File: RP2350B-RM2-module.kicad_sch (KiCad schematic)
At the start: 58 parts, among them J1 SM03B-SRSS-TB, J2 Conn_01x26_Socket, J3 Conn_01x26_Socket, J5 USB_C_Receptacle_USB2.0_16P, SW1 SW_Push, SW2 SW_Push, U1 W25Q128JVSIQ, U2 APS6404L-3SQR-SN, U3 RP2350_80QFN, U4 RM2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

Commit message: clean ERC and DRC
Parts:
- removed U4: RM2, Archbell-KiCad:rpi_rmc20452t, symbol RPI_RMC20452T:RPI_RMC20452T
- added U4: <value>, Archbell-KiCad:rpi_rmc20452t, symbol Archbell-KiCad:RPI_RMC20452T
- U1: symbol Memory_Flash:W25Q128JVS -> Archbell-KiCad:W25Q128JVS
- U2: symbol Memory_Flash:W25Q128JVS -> Archbell-KiCad:W25Q128JVS; JLCPCB C5333729 DNF -> C113767; Part Number APS6404L-3SQR-SN -> W25Q128JVSIQ
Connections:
- net +3V3: now also U4.14 (VDDIO), U4.16 (VIN); no longer U3.23 (GPIO23)
- net GND: now also U5.2 (GND), U4.1 (GND), U4.11 (GND), U4.15 (GND), U4.21 (GND), U4.4 (GND), U4.7 (GND)
- net WL_CLK: now also U4.3 (SCLK)
- net WL_CS: now also U4.9 (CS)
- net WL_DAT: now also U4.5 (DI)
- net WL_GPIO0: now also U4.8 (GPIO0)
- net WL_GPIO1: now also U4.18 (GPIO1)
- net WL_GPIO2: now also U4.17 (GPIO2)
- net at R13.2: now also U4.10 (nIRQ)
- net at R12.2: now also U4.6 (DO)
- net EN renamed 3V3_EN
- new net WL_ON: U3.23 (GPIO23), U4.12 (WL_ON), U4.13 (BT_ON)
- no-connect marks 2 -> 3

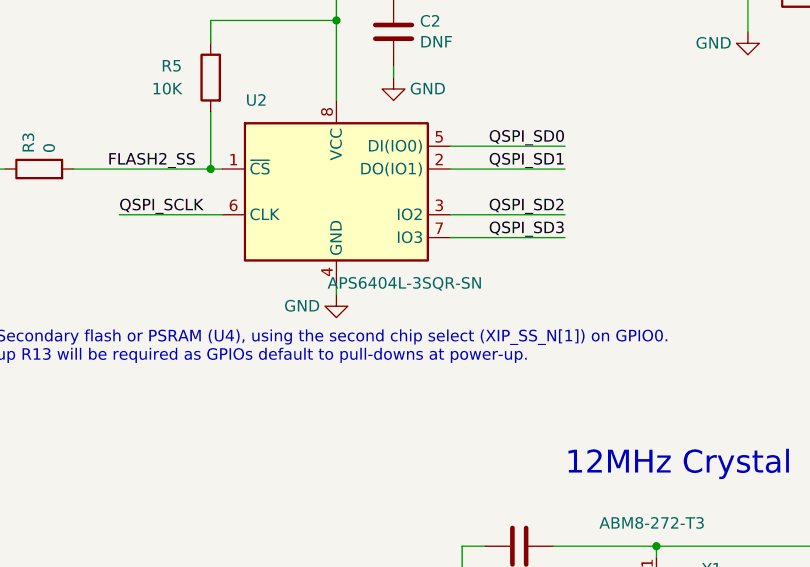
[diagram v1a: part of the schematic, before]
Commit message: Changed PSRAM
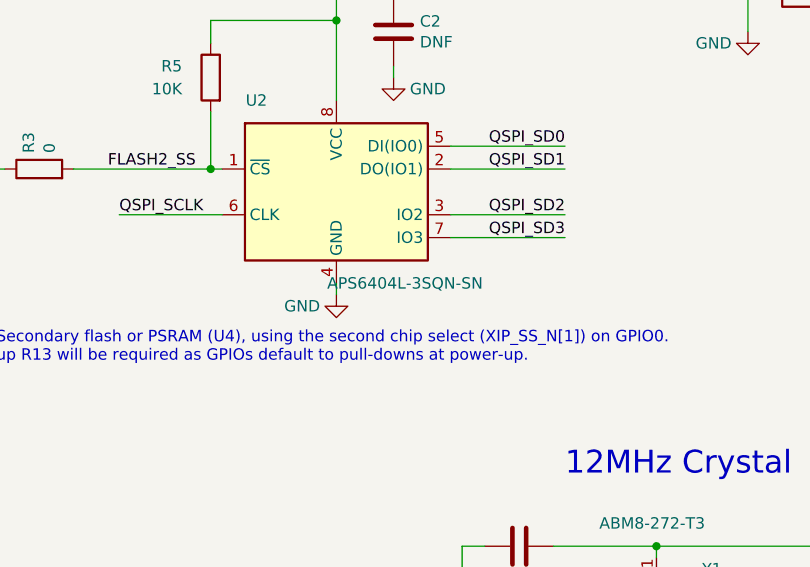
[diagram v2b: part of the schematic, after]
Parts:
- U2: value APS6404L-3SQR-SN -> APS6404L-3SQN-SN
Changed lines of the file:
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@@
 			)
 		)
-		(property "Value" "APS6404L-3SQR-SN"
+		(property "Value" "APS6404L-3SQN-SN"
 			(at 76.2 196.85 0)
 			(show_name no)

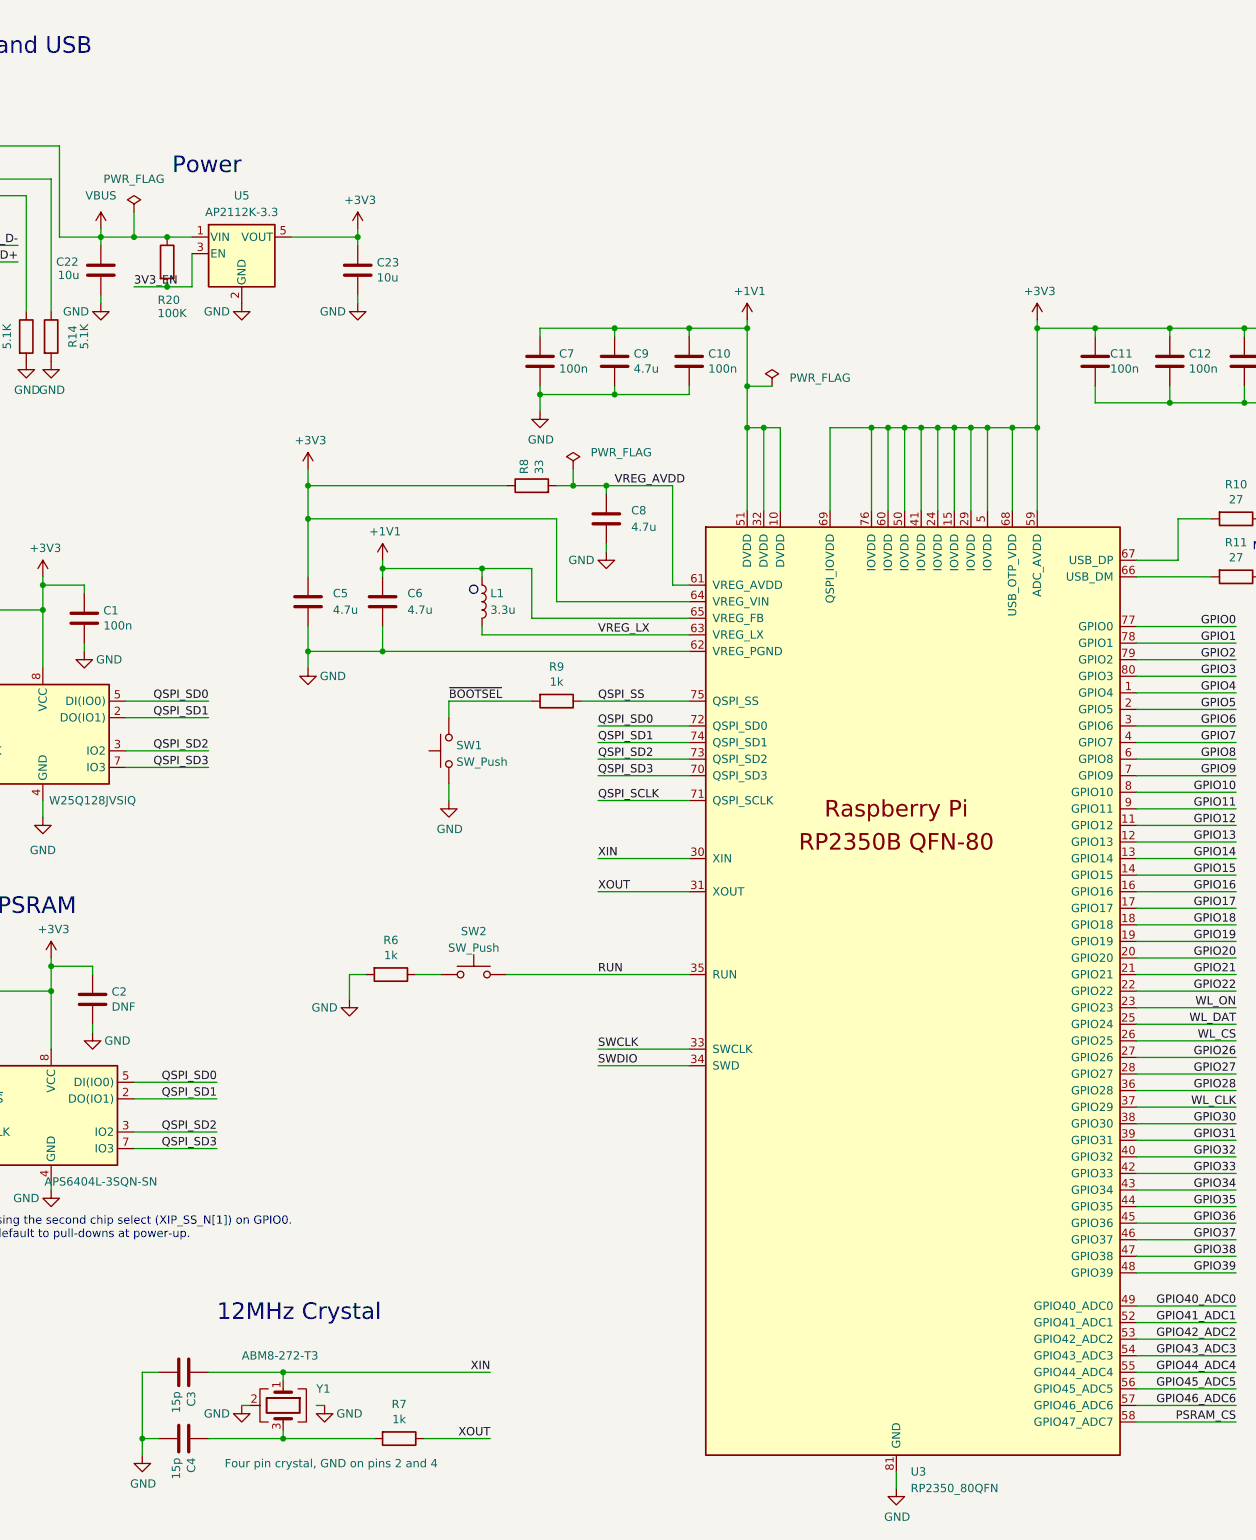
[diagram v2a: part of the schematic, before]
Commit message: Added ADC vref
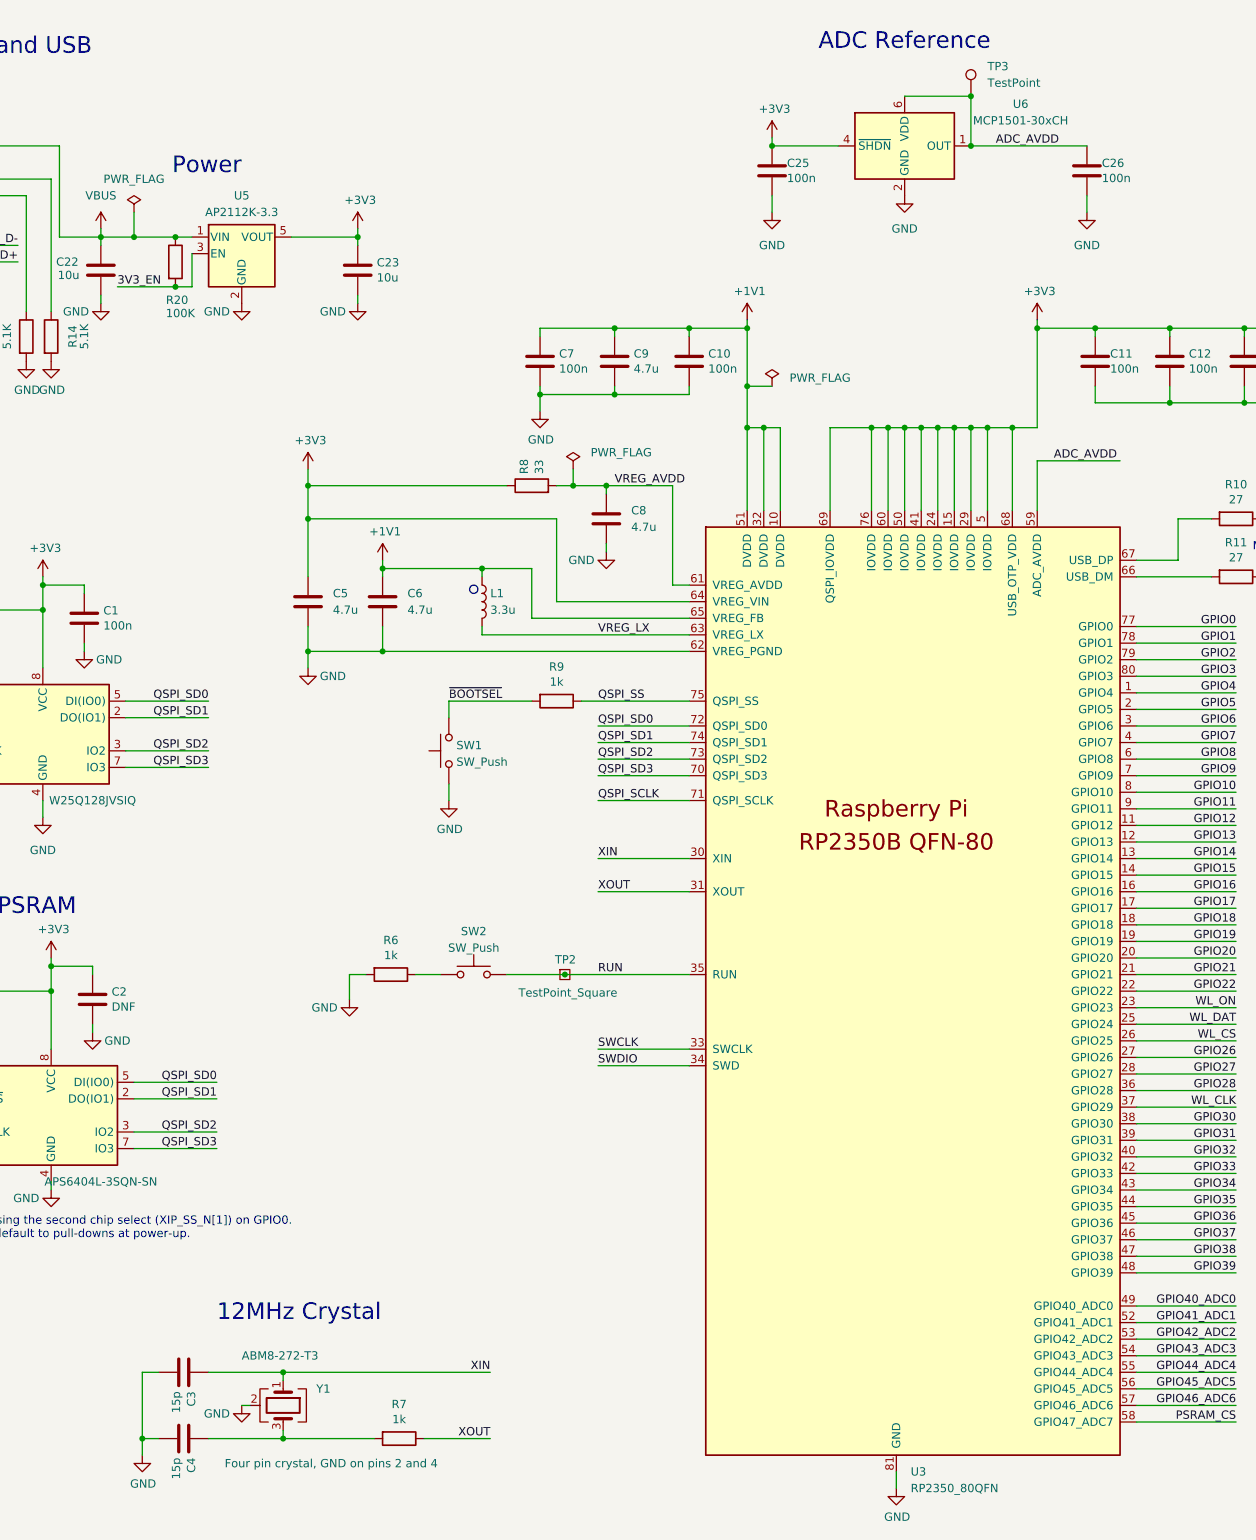
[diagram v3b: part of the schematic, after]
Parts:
- added C25, C26: 100n, Capacitor_SMD:C_0402_1005Metric, symbol Device:C
- added TP2: TestPoint_Square, TestPoint:TestPoint_Pad_1.5x1.5mm, symbol Connector:TestPoint_Square
- added TP3: TestPoint, TestPoint:TestPoint_Pad_D1.5mm, symbol Connector:TestPoint
- added U6: MCP1501-30xCH, Package_TO_SOT_SMD:SOT-23-6, symbol Reference_Voltage:MCP1501-30xCH
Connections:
- net +3V3: now also C25.1, U6.4 (~{SHDN}); no longer U3.59 (ADC_AVDD)
- net GND: now also C25.2, C26.2, U6.2 (GND), U6.3 (GND), U6.5 (GND)
- net RUN: now also TP2.1
- new net ADC_AVDD: C26.1, TP3.1, U3.59 (ADC_AVDD), U6.1 (OUT), U6.6 (VDD)
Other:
- note added: "ADC Reference"
- moved on the sheet: R20

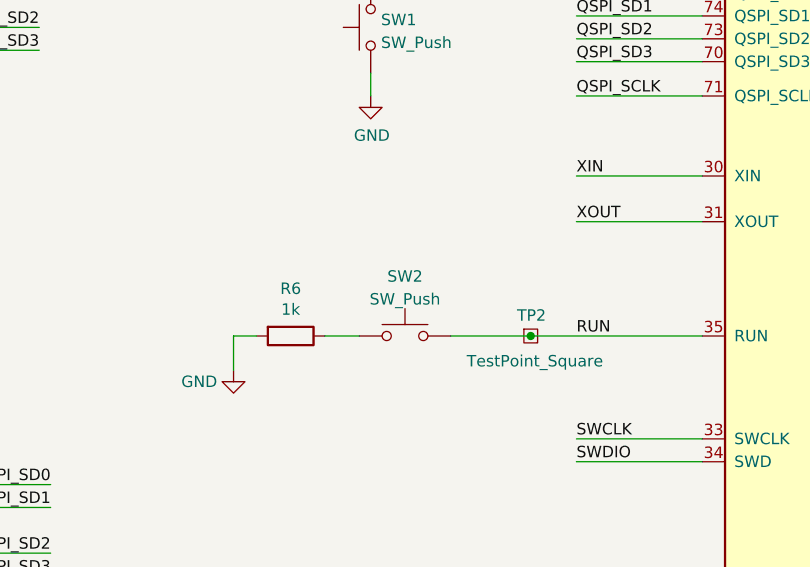
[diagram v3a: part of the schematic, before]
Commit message: Added pin numbering
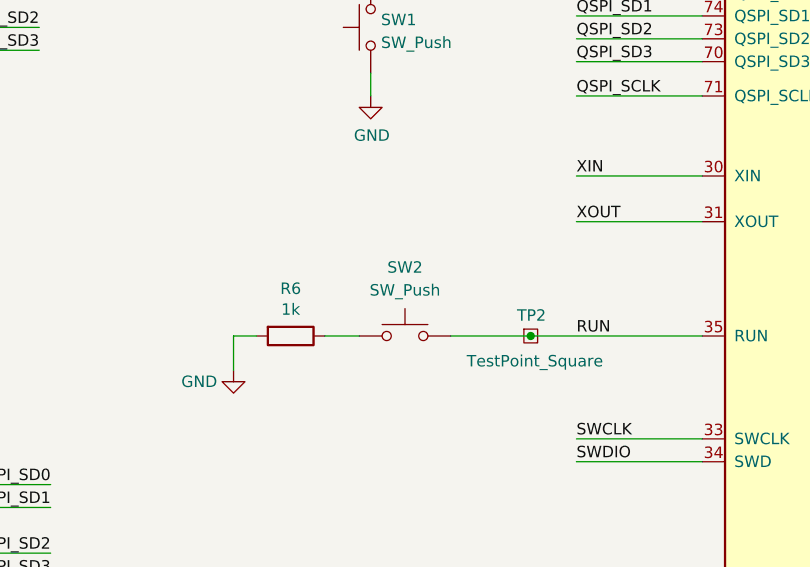
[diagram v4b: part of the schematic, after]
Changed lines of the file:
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@@
 		(fields_autoplaced yes)
 		(property "Reference" "SW2"
-			(at 133.35 158.4792 0)
+			(at 133.35 157.48 0)
 			(show_name no)
 			(do_not_autoplace no)
@@
 		)
 		(property "Value" "SW_Push"
-			(at 133.35 161.0161 0)
+			(at 133.35 160.02 0)
 			(show_name no)
 			(do_not_autoplace no)
